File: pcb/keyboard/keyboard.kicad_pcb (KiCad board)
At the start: 2 copper layers, 137.2 x 109.2 mm, 71 parts, among them J1 Audio-Jack-4, J2 sidebutton, SW1 RESET_SW, U1 Arduino_Pro_Micro, U2 Arduino_Pro_Micro

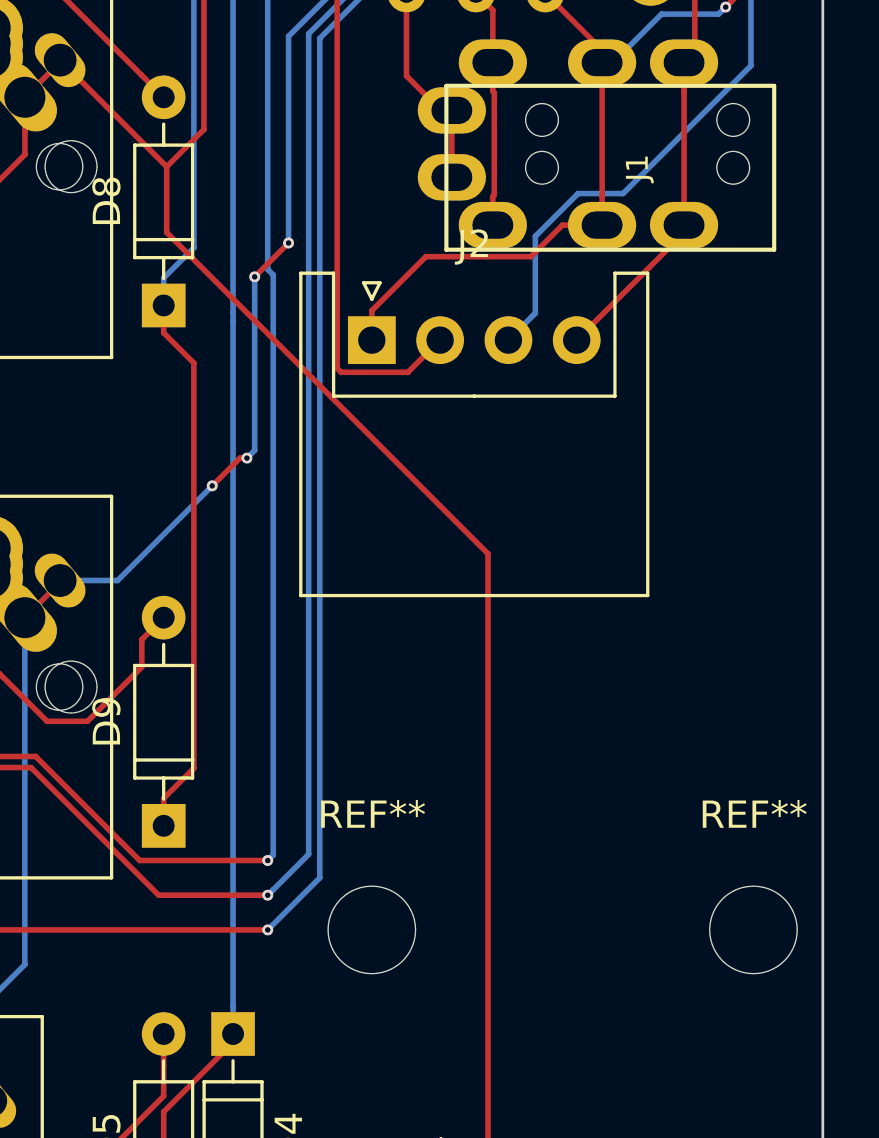
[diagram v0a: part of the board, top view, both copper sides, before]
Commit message: sidebutton conn: XH -> Wirepad
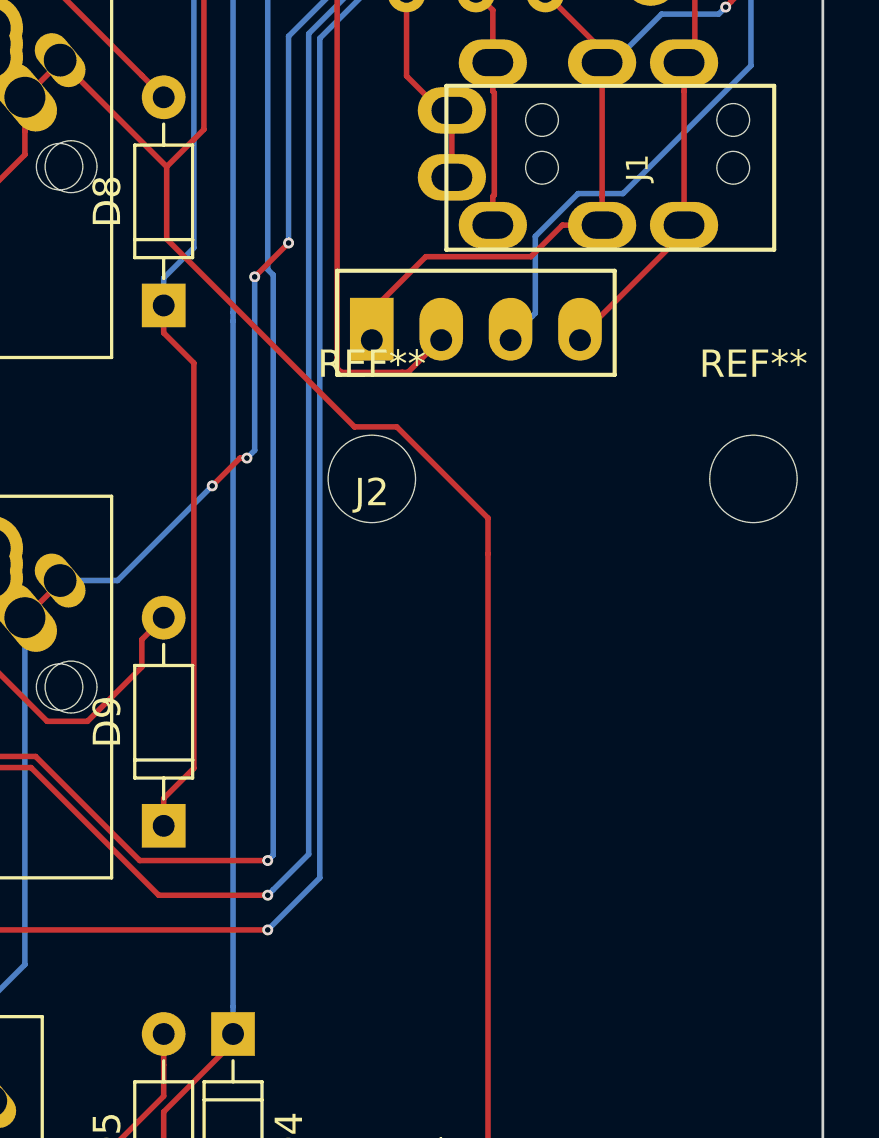
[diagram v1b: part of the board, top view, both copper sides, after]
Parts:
- J2: footprint Connectors_JST:JST_XH_S04B-XH-A_04x2.50mm_Angled -> 4x6t2:Wirepad_01x04
- moved REF** 16.5 mm to (134.6, 57.1)
- moved REF** 16.5 mm to (120.7, 57.1)
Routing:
- net /ROW2: track 280.4 -> 281.3 mm

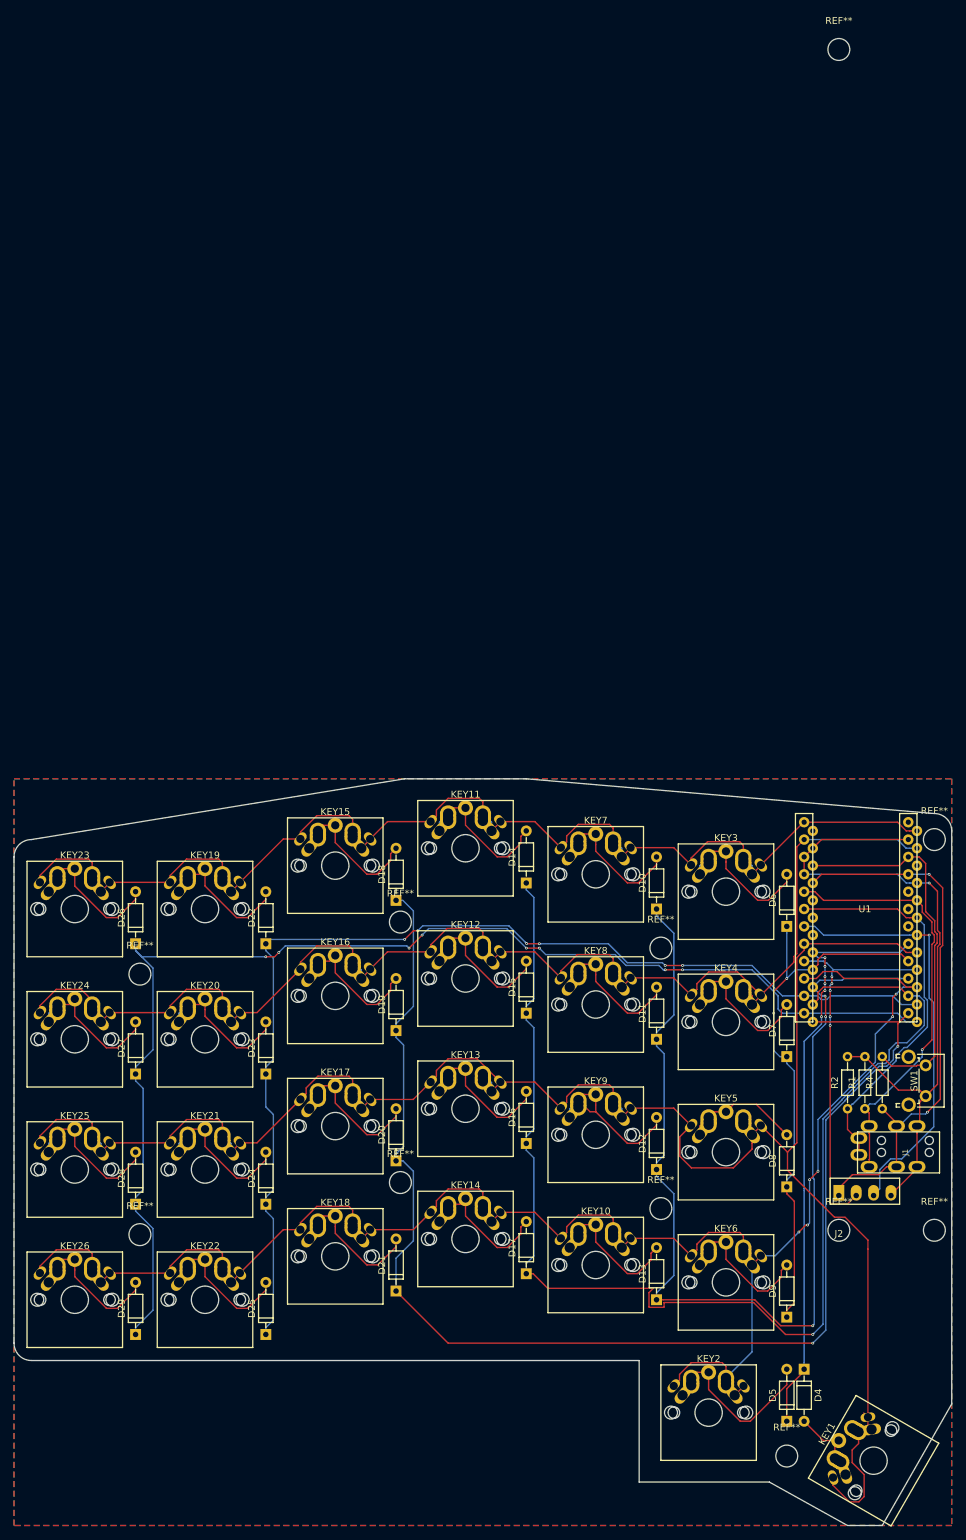
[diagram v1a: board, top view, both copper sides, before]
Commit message: switching diode: THT -> SMD
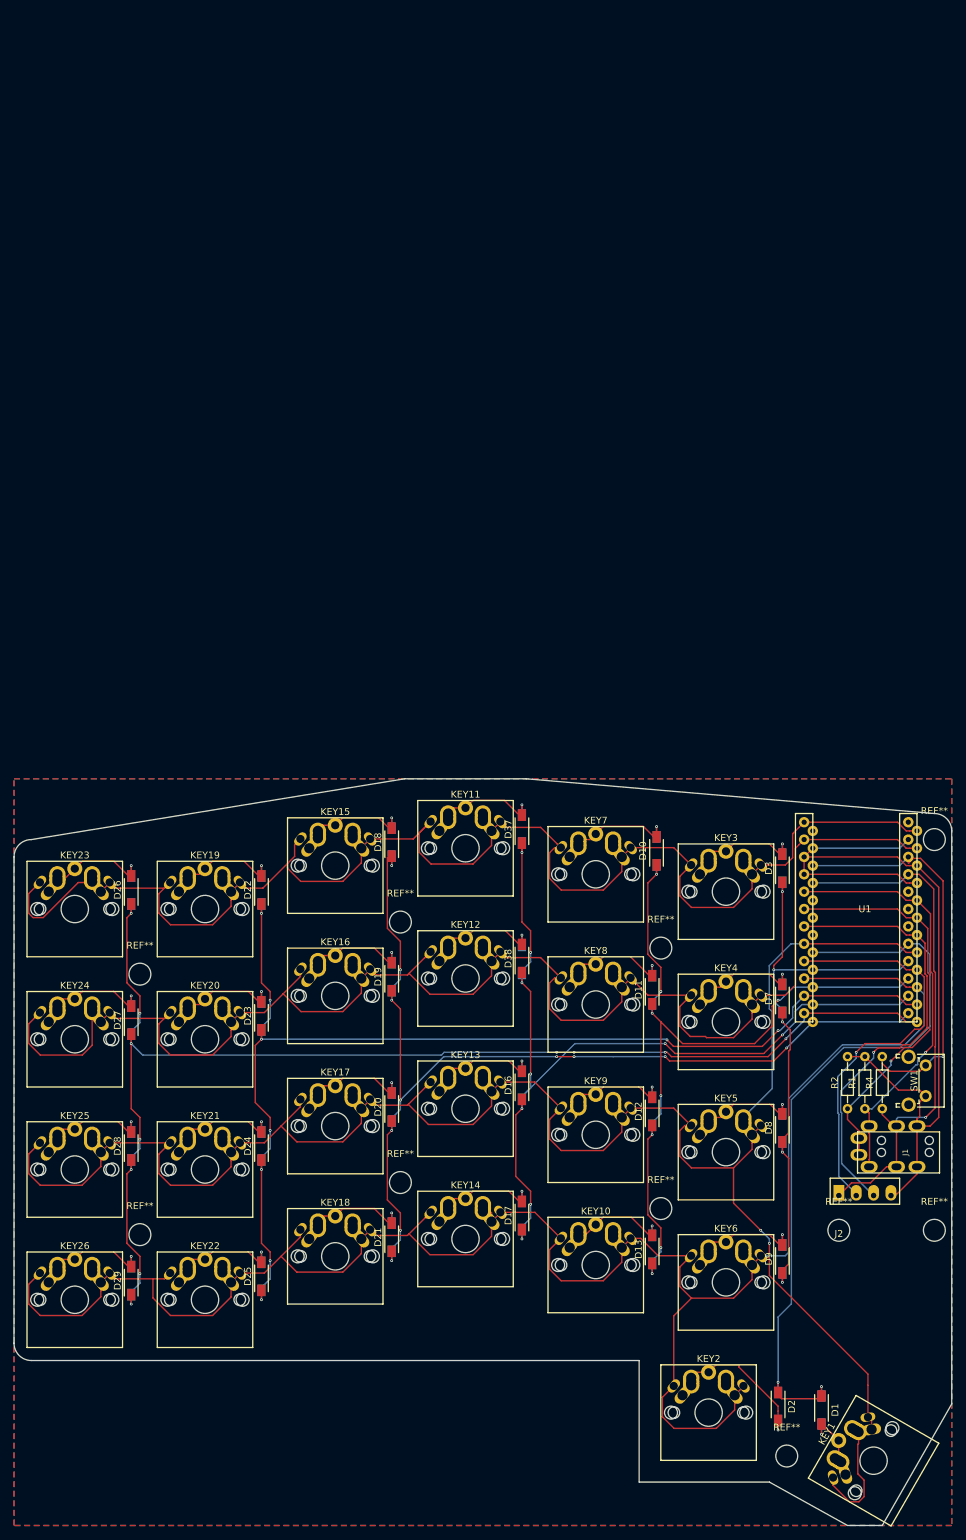
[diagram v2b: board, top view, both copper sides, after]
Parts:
- removed the REF** at (120.7, -115.6)
- added D1: D, 4x6t2:D_SOD-123, F.Cu at (118.1, 83.4)
- added D2: D, 4x6t2:D_SOD-123, F.Cu at (111.8, 82.9)
- added D3: D, 4x6t2:D_SOD-123, F.Cu at (112.4, 4.19)
- added D30: D, 4x6t2:D_SOD-123, B.Cu at (112.4, 23.2)
- added D31: D, 4x6t2:D_SOD-123, B.Cu at (112.4, 42.2)
- added D32: D, 4x6t2:D_SOD-123, B.Cu at (112.4, 61.3)
- added D33: D, 4x6t2:D_SOD-123, B.Cu at (94.0, 1.65)
- added D34: D, 4x6t2:D_SOD-123, B.Cu at (93.3, 22.0)
- added D35: D, 4x6t2:D_SOD-123, B.Cu at (93.3, 39.8)
- added D36: D, 4x6t2:D_SOD-123, B.Cu at (93.3, 59.9)
- added D37: D, 4x6t2:D_SOD-123, F.Cu at (74.3, -1.52)
- added D38: D, 4x6t2:D_SOD-123, F.Cu at (74.3, 17.4)
- added D39: D, 4x6t2:D_SOD-123, B.Cu at (74.3, 35.9)
- added D40: D, 4x6t2:D_SOD-123, B.Cu at (74.3, 55.0)
- added D41: D, 4x6t2:D_SOD-123, B.Cu at (55.2, 0.38)
- added D42: D, 4x6t2:D_SOD-123, B.Cu at (55.2, 20.1)
- added D43: D, 4x6t2:D_SOD-123, B.Cu at (55.2, 39.1)
- added D44: D, 4x6t2:D_SOD-123, B.Cu at (55.2, 58.2)
- added D45: D, 4x6t2:D_SOD-123, B.Cu at (36.2, 7.37)
- added D46: D, 4x6t2:D_SOD-123, B.Cu at (36.2, 25.8)
- added D47: D, 4x6t2:D_SOD-123, B.Cu at (36.2, 44.8)
- added D48: D, 4x6t2:D_SOD-123, B.Cu at (36.2, 63.9)
- added D49: D, 4x6t2:D_SOD-123, B.Cu at (17.1, 7.37)
- added D50: D, 4x6t2:D_SOD-123, B.Cu at (17.1, 26.4)
- added D51: D, 4x6t2:D_SOD-123, B.Cu at (17.1, 44.8)
- added D52: D, 4x6t2:D_SOD-123, B.Cu at (17.1, 64.5)
- D10, D11, D12, D13, D16, D17, D18, D19, D20, D21, D22, D23, D24, D25, D26, D27, D28, D29, D7, D8, D9: footprint Diodes_THT:D_DO-35_SOD27_P7.62mm_Horizontal -> 4x6t2:D_SOD-123
- D14, D15, D4, D5, D6: footprint Diodes_THT:D_DO-35_SOD27_P7.62mm_Horizontal -> 4x6t2:D_SOD-123; moved to B.Cu
- moved D8 8.66 mm to (112.4, 42.2)
- moved D16 8.53 mm to (74.3, 35.9)
- moved D24 8.53 mm to (36.2, 44.8)
- moved D28 8.53 mm to (17.1, 44.8)
- moved D7 8.53 mm to (112.4, 23.2)
- moved D18 8.53 mm to (55.2, 0.38)
- moved D12 8.53 mm to (93.3, 39.8)
- moved D17 8.53 mm to (74.3, 55.0)
- moved D23 8.53 mm to (36.2, 25.8)
- moved D25 8.53 mm to (36.2, 63.9)
- moved D6 8.53 mm to (112.4, 4.19)
- moved D9 8.53 mm to (112.4, 61.3)
- moved D10 8.51 mm to (94.0, 1.65)
- moved D21 7.90 mm to (55.2, 58.2)
- moved D14 7.90 mm to (74.3, -1.52)
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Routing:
- net /ROW4: track 246.6 -> 299.3 mm, vias 6 -> 0
- net /COL3: track 184.8 -> 136.0 mm, vias 1 -> 9
- net /ROW0: track 172.1 -> 216.6 mm
- net /COL4: track 195.0 -> 153.4 mm, vias 2 -> 11
- net /ROW1: track 192.7 -> 234.2 mm
- net /COL2: track 152.7 -> 115.1 mm, vias 3 -> 8
- net /COL0: track 86.8 -> 109.6 mm, vias 6 -> 2
- net GND: track 103.4 -> 125.6 mm, vias 1 -> 0
- net /ROW2: track 281.3 -> 300.3 mm, vias 0 -> 2
- net /COL5: track 161.5 -> 170.1 mm, vias 6 -> 9
- net /COL1: track 81.3 -> 89.1 mm, vias 2 -> 5
- net Net-(D12-Pad2): track 24.8 -> 18.2 mm, vias 0 -> 1
- net Net-(D27-Pad2): track 23.5 -> 18.4 mm, vias 0 -> 1
- net /X: track 55.6 -> 60.4 mm, vias 5 -> 1
- net /COL6: track 185.7 -> 190.1 mm, vias 8 -> 11
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
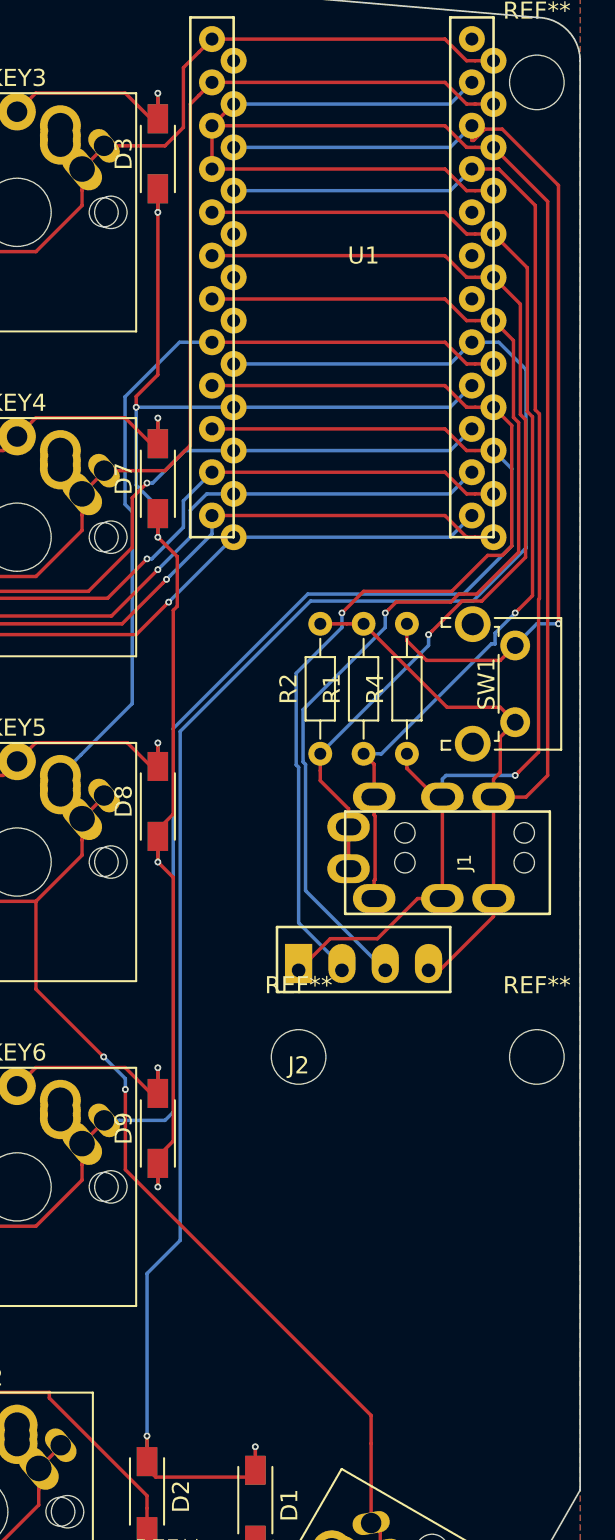
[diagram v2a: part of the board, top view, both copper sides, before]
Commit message: i2c: pull down -> pull up
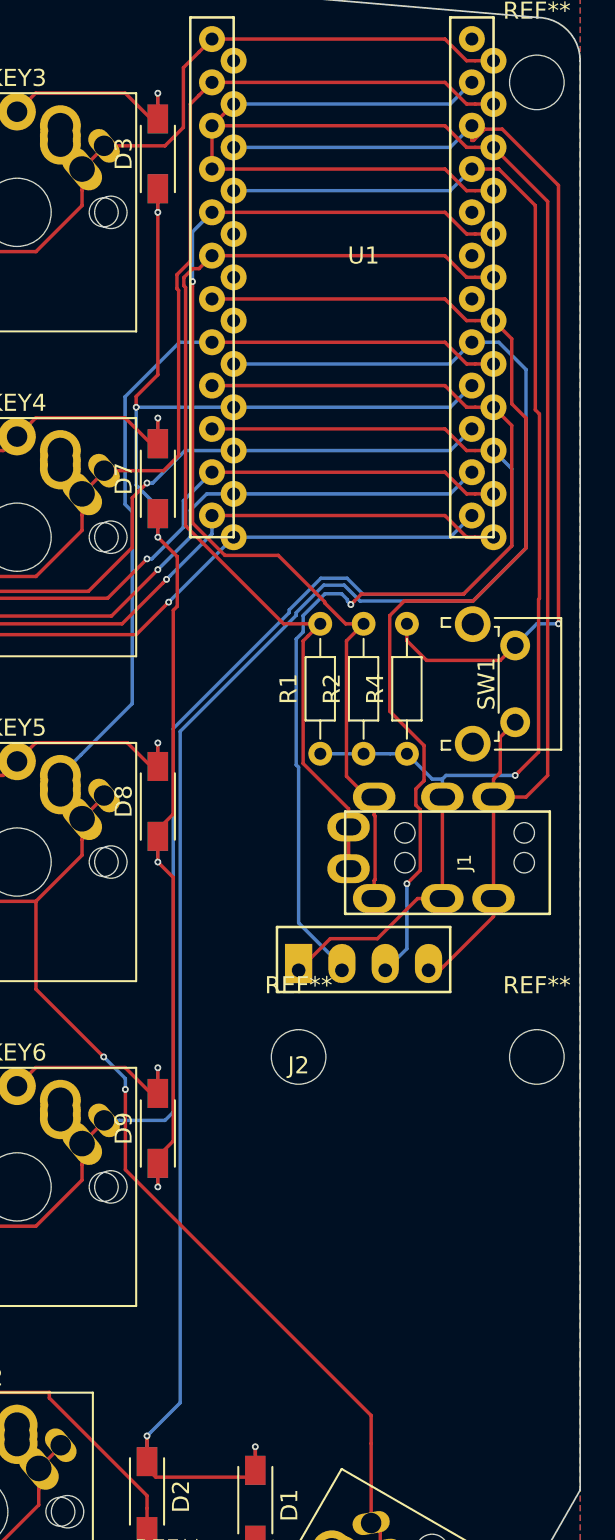
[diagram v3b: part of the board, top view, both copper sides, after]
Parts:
- moved R1 2.54 mm to (121.9, 39.4)
- moved R2 2.54 mm to (124.5, 39.4)
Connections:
- R1 pad 1: /SDA -> +5V
- R1 pad 2: GND -> /SCL
- R2 pad 1: /SCL -> +5V
- R2 pad 2: GND -> /SDA
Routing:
- net GND: track 125.6 -> 111.8 mm
- net +5V: track 78.4 -> 82.9 mm
- net /SDA: track 62.1 -> 65.7 mm
- net /Y: track 65.5 -> 63.6 mm
- net /X: track 60.4 -> 62.2 mm
- net /SCL: track 58.8 -> 60.0 mm, vias 1 -> 0
- net /COL0: track 109.6 -> 110.5 mm
- net /ROW4: track 299.3 -> 300.2 mm
